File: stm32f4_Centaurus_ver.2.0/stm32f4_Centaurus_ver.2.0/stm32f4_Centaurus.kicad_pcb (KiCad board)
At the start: 2 copper layers, 100 x 79 mm, 207 parts, among them IC1 PIC24FJ64GB004, P1 PICKit3, P10 XA2_12V, P11 CAN0, P12 CAN1, P13 CAN0, P14 CAN1, P15 SERIAL2, P16 SERIAL0, P17 XA2_5V, P18 SWD, P2 SERIAL5_SBDBT, P23 A/D, P24 PWM, P25 A/D_batt, P26 PWM_batt, P27 EMERGENCY_CHECK, P28 I/O_5V, P29 I/O_Variable, P3 ENC0, P30 I/O_5V_batt, P31 I/O_Variable, P4 ENC2, P5 SERIAL1, P6 ENC3, P7 ENC1, P8 SERIAL4, P9 SERIAL3, Q1 FET_P, Q2 FET_P, Q3 FET_P, Q4 NPN, Q5 NPN, Q6 FET_P, Q7 FET_N, SW1 Main_POWER, SW2 SW1, SW3 SW0, SW4 SW2, SW5 SW3, U1 STM32F407VG, U10 LOGO, U12 25LC010A, U13 LOGO, U2 AZ1086H, U3 MCP2221A, U4 AP3211, U5 MAX3051, U6 MAX3051, U7 AQM1602_BL, U8 OSTBABS4C2B, U9 LOGO, X1 8MHz

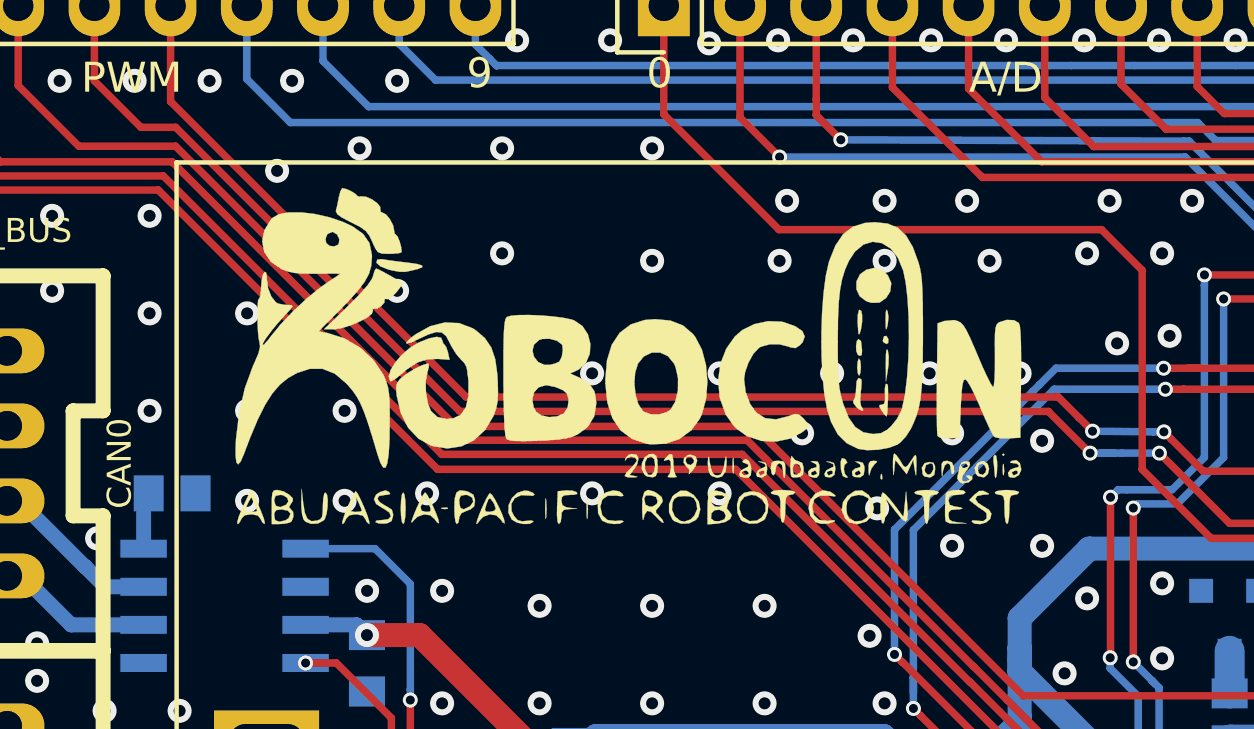
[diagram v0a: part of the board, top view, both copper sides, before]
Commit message: mainと電源が仮完成.
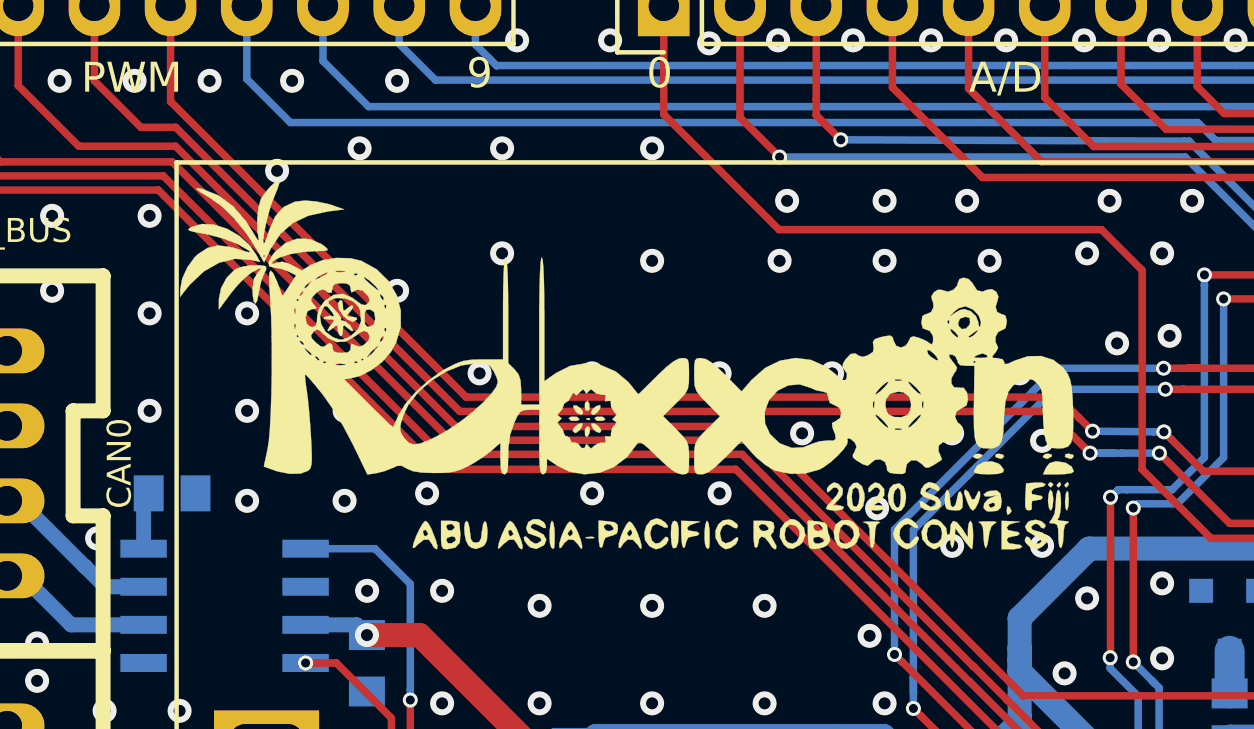
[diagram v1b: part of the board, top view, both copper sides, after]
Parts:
- U13: footprint Mizz_lib:Robocon2019_30.0x30.0_silk -> Mizz_lib:Robocon2020_30.0x12.5_silk
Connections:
- C11 pad 1: Net-(C11-Pad1) -> /OSC_OUT
- C13 pad 1: Net-(C13-Pad1) -> /OSC_IN
- R18 pad 1: Net-(R18-Pad1) -> Net-(P6-Pad4)
- R19 pad 1: Net-(R19-Pad1) -> Net-(P7-Pad4)
- R8 pad 1: Net-(R8-Pad1) -> Net-(P3-Pad4)
- R9 pad 1: Net-(R9-Pad1) -> Net-(P4-Pad4)

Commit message: main基板のdcdc改善
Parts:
- R35: value 50k -> 3.9k
- R36: value 10k -> 680
- U4: value AP3211 -> BD9G101G
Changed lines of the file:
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@@
       (effects (font (size 1 1) (thickness 0.15)) (justify mirror))
     )
-    (fp_text value AP3211 (at 0.5 2.5 270) (layer B.SilkS)
+    (fp_text value BD9G101G (at 0.5 2.5 270) (layer B.SilkS)
       (effects (font (size 0.8 0.8) (thickness 0.15)) (justify mirror))
     )
@@
       (effects (font (size 1 1) (thickness 0.15)) (justify mirror))
     )
-    (fp_text value FET_P (at 3.75 0 90) (layer B.SilkS)
-      (effects (font (size 1 1) (thickness 0.15)) (justify mirror))
+    (fp_text value FET_P (at 0 -2.15 90) (layer B.SilkS)
+      (effects (font (size 0.8 0.8) (thickness 0.15)) (justify mirror))
     )
     (fp_line (start -1.65 1.6) (end 1.65 1.6) (layer B.CrtYd) (width 0.05))
@@
       (effects (font (size 1 1) (thickness 0.15)) (justify mirror))
     )
-    (fp_text value 10k (at 3 0 270) (layer B.SilkS)
-      (effects (font (size 1 1) (thickness 0.15)) (justify mirror))
+    (fp_text value 10k (at 0 -1.4 270) (layer B.SilkS)
+      (effects (font (size 0.8 0.8) (thickness 0.15)) (justify mirror))
     )
     (fp_line (start -1.3 0.8) (end 1.3 0.8) (layer B.CrtYd) (width 0.05))
@@
       (effects (font (size 1 1) (thickness 0.15)) (justify mirror))
     )
-    (fp_text value 50k (at 2.75 0 180) (layer B.SilkS)
+    (fp_text value 3.9k (at 3.1 0 180) (layer B.SilkS)
       (effects (font (size 1 1) (thickness 0.15)) (justify mirror))
     )
@@
       (effects (font (size 1 1) (thickness 0.15)) (justify mirror))
     )
-    (fp_text value 10k (at -2.55 -0.35 180) (layer B.SilkS)
+    (fp_text value 680 (at -2.55 -0.35 180) (layer B.SilkS)
       (effects (font (size 0.8 0.8) (thickness 0.15)) (justify mirror))
     )

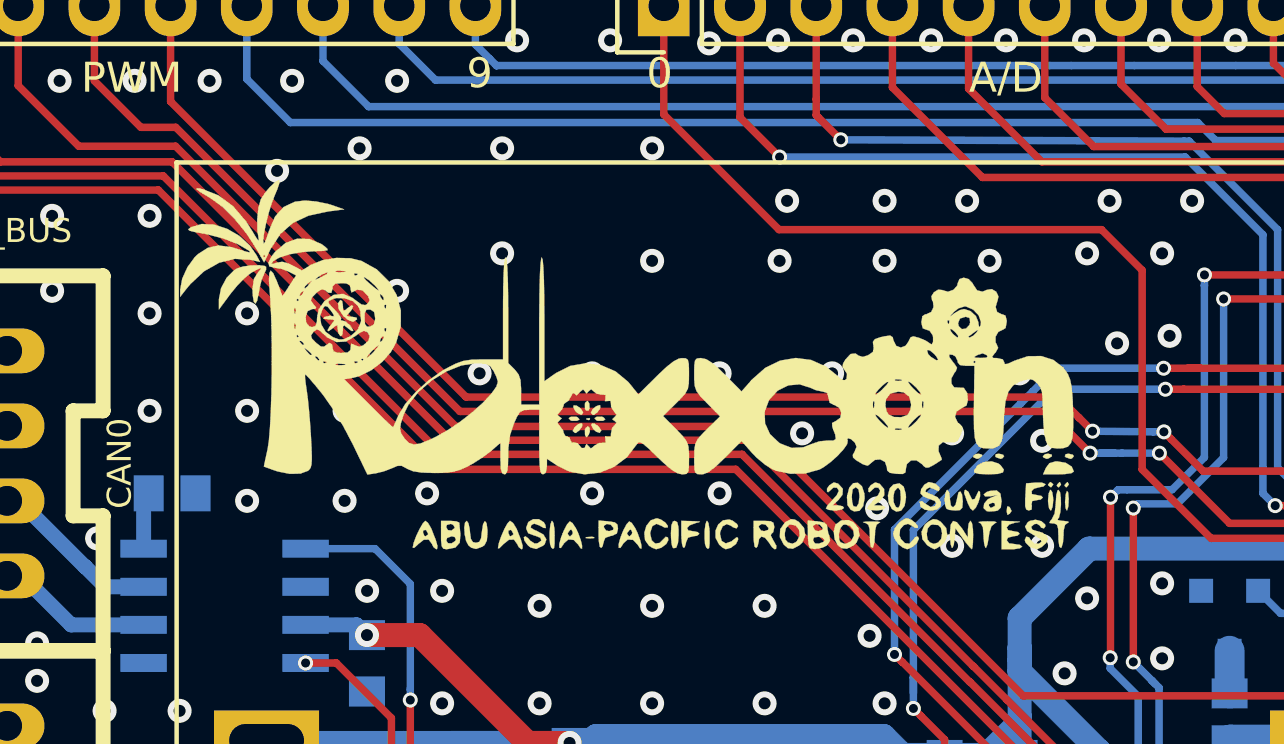
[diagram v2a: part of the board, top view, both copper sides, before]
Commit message: パワー系の配線完了かな
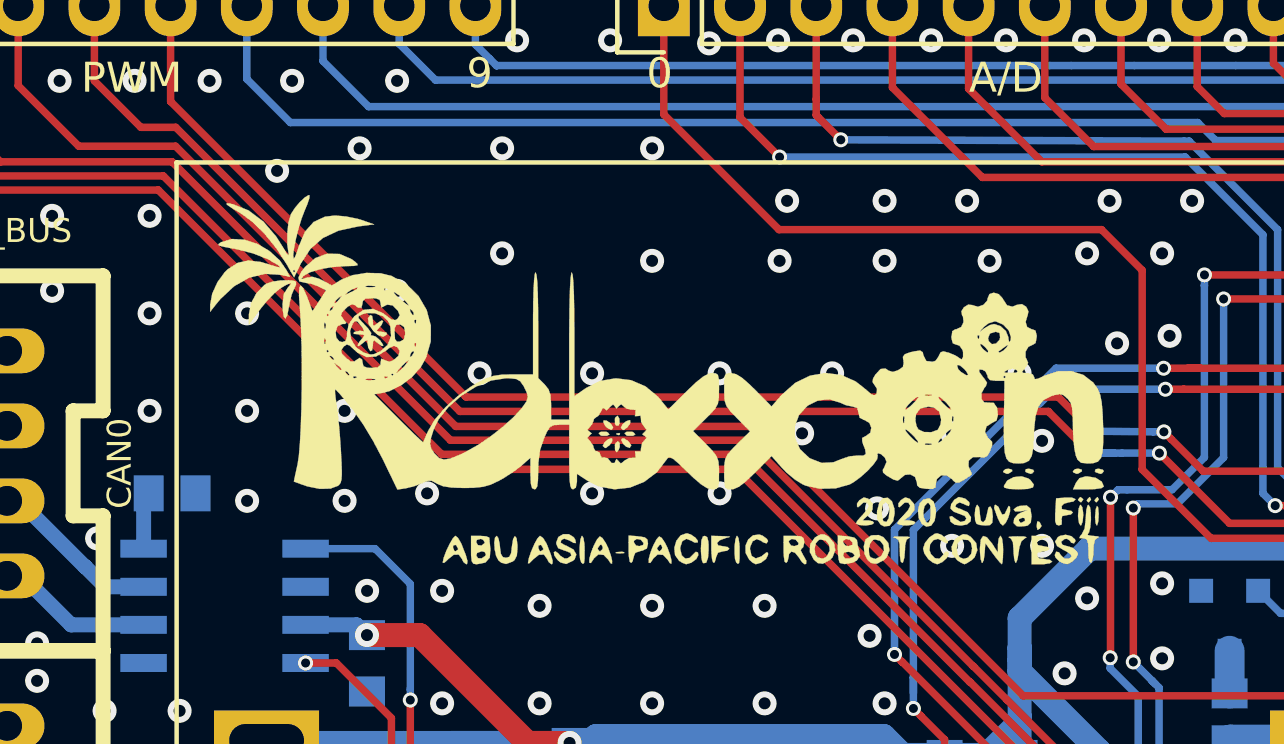
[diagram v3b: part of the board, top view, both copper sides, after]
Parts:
- R53: value 120 -> 10
- moved U13 1.12 mm to (90.8, 79.2)
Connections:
- C22 pad 2: Net-(C22-Pad2) -> CAN0_BUS_Vdd
- C23 pad 2: Net-(C23-Pad2) -> CAN1_BUS_Vdd
- R71 pad 1: Net-(R71-Pad1) -> Net-(P27-Pad4)
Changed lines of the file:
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@@
     (zones 0)
     (modules 207)
-    (nets 223)
+    (nets 220)
   )
   (page A4)
@@
   (net 218 "Net-(Q4-Pad3)")
   (net 219 +3V3)
-  (net 220 "Net-(C22-Pad2)")
-  (net 221 "Net-(C23-Pad2)")
-  (net 222 "Net-(R71-Pad1)")
   (net_class Default "これはデフォルトのネット クラスです。"
     (clearance 0.2)
@@
     (add_net "Net-(C18-Pad2)")
     (add_net "Net-(C19-Pad1)")
-    (add_net "Net-(C22-Pad2)")
-    (add_net "Net-(C23-Pad2)")
     (add_net "Net-(C26-Pad1)")
     (add_net "Net-(C27-Pad1)")
@@
     (add_net "Net-(R63-Pad2)")
     (add_net "Net-(R64-Pad2)")
-    (add_net "Net-(R71-Pad1)")
     (add_net "Net-(U3-Pad10)")
     (add_net "Net-(U3-Pad8)")
@@
       (effects (font (size 1 1) (thickness 0.15)) (justify mirror))
     )
-    (fp_text value BD9G101G (at 0.5 2.5 270) (layer B.SilkS)
+    (fp_text value BD9G101G (at 1.5 2.5 270) (layer B.SilkS)
       (effects (font (size 0.8 0.8) (thickness 0.15)) (justify mirror))
     )
@@
       (net 2 GND))
     (pad 2 smd rect (at 0.93 0 270) (size 1 1.2) (layers B.Cu B.Paste B.Mask)
-      (net 220 "Net-(C22-Pad2)"))
+      (net 184 CAN0_BUS_Vdd))
     (model C:/Users/Mizuta/Downloads/kicad-packages3D-master/Capacitor_SMD.3dshapes/C_0603_1608Metric.step
       (at (xyz 0 0 0))
@@
     (fp_line (start -0.8 -0.4) (end -0.8 0.4) (layer B.Fab) (width 0.15))
     (pad 2 smd rect (at 0.93 0 270) (size 1 1.2) (layers B.Cu B.Paste B.Mask)
-      (net 221 "Net-(C23-Pad2)"))
+      (net 185 CAN1_BUS_Vdd))
     (pad 1 smd rect (at -0.95 0 270) (size 1 1.2) (layers B.Cu B.Paste B.Mask)
       (net 2 GND))
@@
       (effects (font (size 1 1) (thickness 0.15)) (justify mirror))
     )
-    (fp_text value 120 (at 0 1.5) (layer B.SilkS)
+    (fp_text value 10 (at 0 1.5) (layer B.SilkS)
       (effects (font (size 1 1) (thickness 0.15)) (justify mirror))
     )
@@
     (fp_line (start -0.5 0.675) (end 0.5 0.675) (layer B.SilkS) (width 0.15))
     (pad 1 smd rect (at -0.78 0) (size 1 1.2) (layers B.Cu B.Paste B.Mask)
-      (net 222 "Net-(R71-Pad1)"))
+      (net 206 "Net-(P27-Pad4)"))
     (pad 2 smd rect (at 0.78 0) (size 1 1.2) (layers B.Cu B.Paste B.Mask)
       (net 2 GND))
@@
   )
   (module Mizz_lib:Robocon2020_30.0x12.5_silk (layer F.Cu)
-    (at 89.75 78.75)
+    (at 90.75 79.25)
     (fp_text reference U13 (at 0 0) (layer F.SilkS) hide
       (effects (font (size 1.524 1.524) (thickness 0.3)))

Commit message: 2020/01/04
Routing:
- net GND: vias 450 -> 393

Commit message: 2020/01/07の進捗
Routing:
- net GND: vias 393 -> 392
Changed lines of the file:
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@@
     (thickness 1.6)
     (drawings 137)
-    (tracks 2725)
+    (tracks 2724)
     (zones 0)
     (modules 207)
@@
   (via (at 80.75 71.5) (size 0.8) (drill 0.4) (layers F.Cu B.Cu) (net 2))
   (via (at 94.75 75.25) (size 0.8) (drill 0.4) (layers F.Cu B.Cu) (net 2))
-  (via (at 88.25 83) (size 0.8) (drill 0.4) (layers F.Cu B.Cu) (net 2))
   (via (at 92.75 79) (size 0.8) (drill 0.4) (layers F.Cu B.Cu) (net 2))
   (via (at 103.5 84.75) (size 0.8) (drill 0.4) (layers F.Cu B.Cu) (net 2))
